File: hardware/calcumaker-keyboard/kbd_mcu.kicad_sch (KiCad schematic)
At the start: 8 parts, among them J2 SWD TC2030-NL, U1 STM32G031K8U6

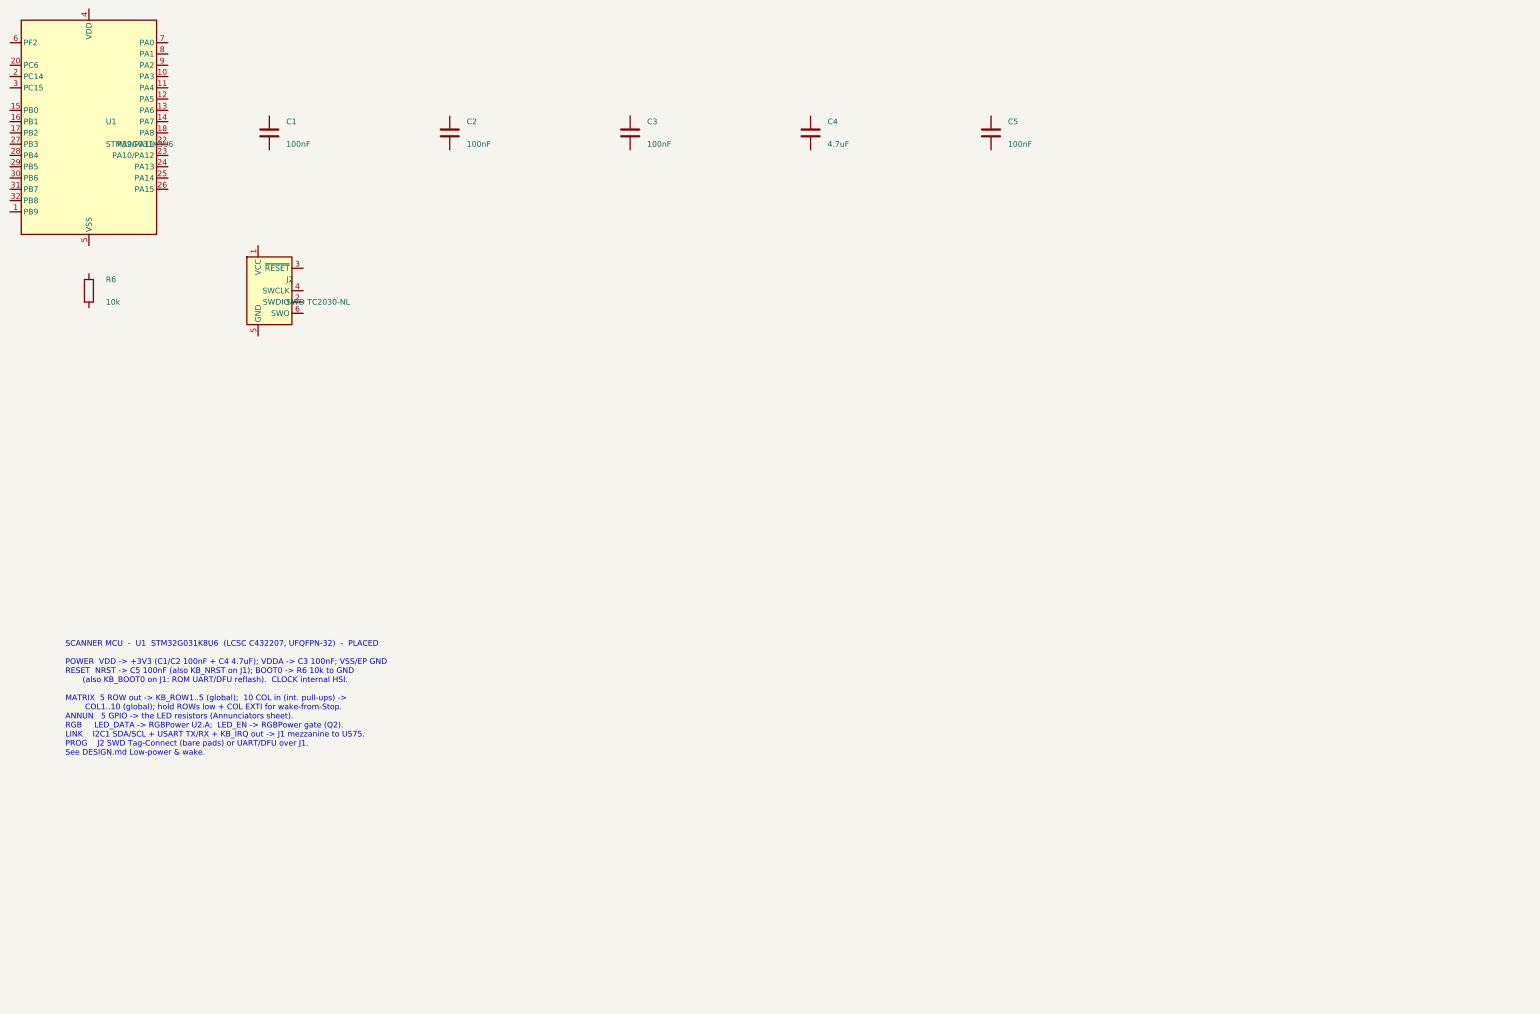
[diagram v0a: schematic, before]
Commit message: Wire mainboard and keypad schematics and verify expanded nets
Connect hierarchical interfaces, power/control circuits, debug links, matrix and RGB chains. Correct MCU package pins, diode polarity and power configuration; add bypass components and repeatable KiCad netlist/ERC checks. Document pin maps and remaining physical validation.
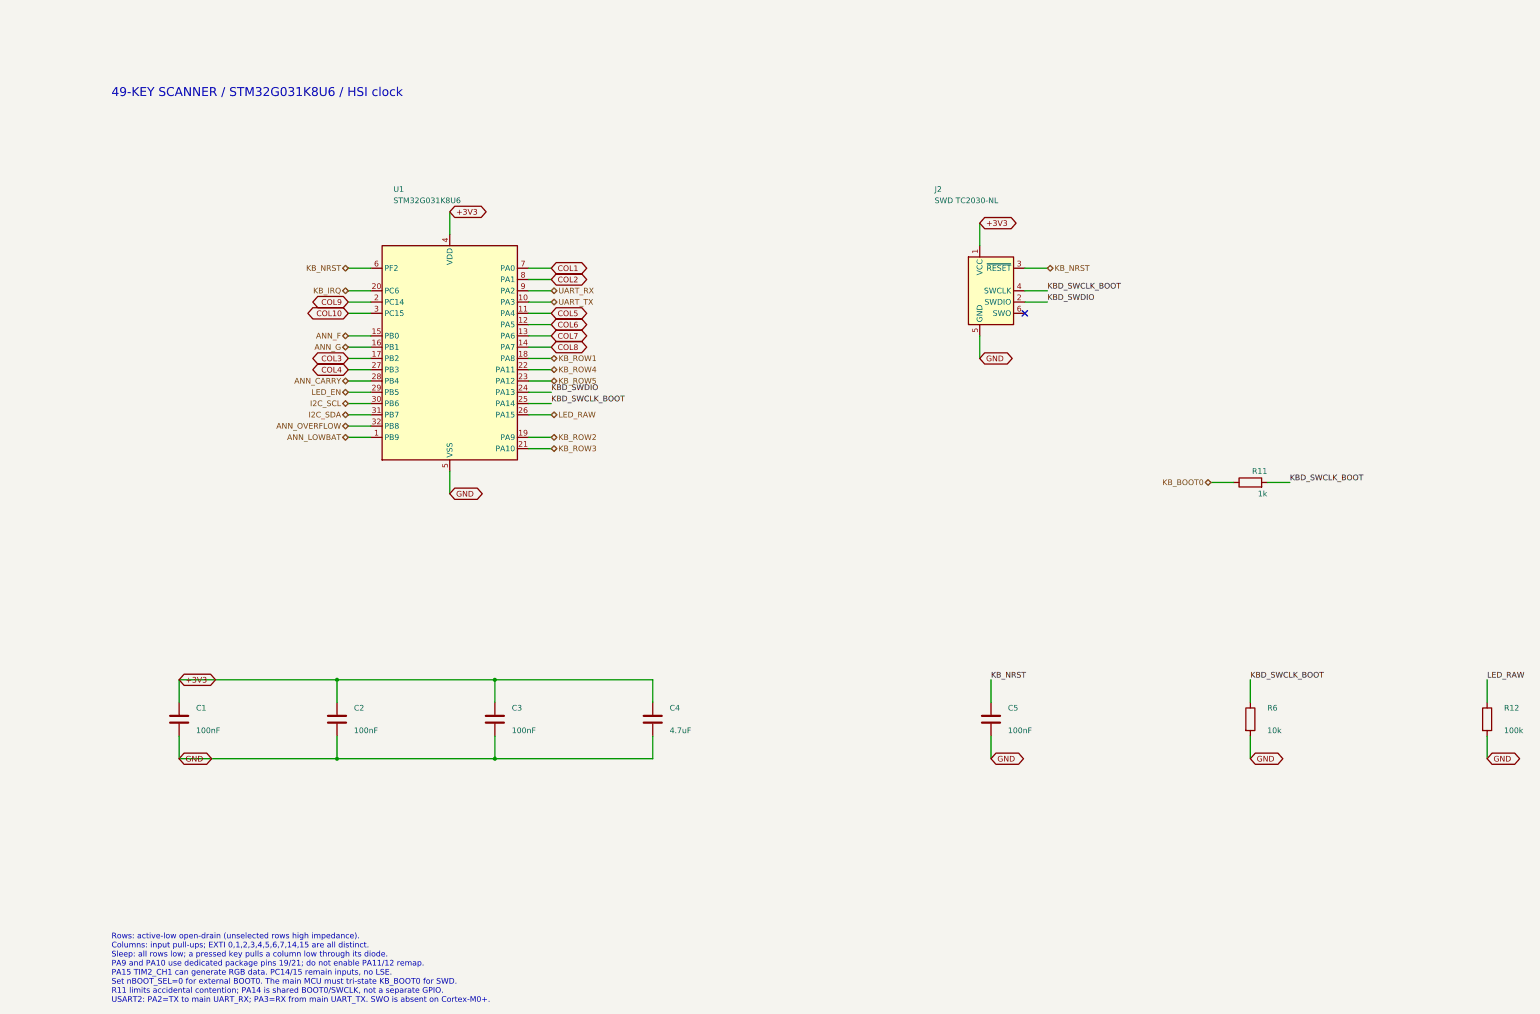
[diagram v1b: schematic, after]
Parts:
- added R11: 1k, Resistor_SMD:R_0402_1005Metric, symbol Device:R
- added R12: 100k, Resistor_SMD:R_0402_1005Metric, symbol Device:R
- U1: symbol MCU_ST_STM32G0:STM32G031K8Ux -> calcumaker:STM32G031K8U6
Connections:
- net +3V3: now reaches C2.1
- net +3V3: now also C1.1, C3.1, C4.1, J2.1 (VCC), U1.4 (VDD)
- net GND: now reaches C2.2
- net GND: now also C1.2, C3.2, C4.2, C5.2, J2.5 (GND), R6.2, U1.33 (VSS), U1.5 (VSS), R12.2
- net KBD_SWDIO: now reaches J2.2 (SWDIO)
- net KBD_SWDIO: now also U1.24 (PA13)
- net KB_NRST: now reaches J2.3 (~{RESET})
- net KB_NRST: now also C5.1, U1.6 (PF2)
- net KBD_SWCLK_BOOT: now reaches J2.4 (SWCLK)
- net KBD_SWCLK_BOOT: now also R6.1, U1.25 (PA14), R11.2
- net ANN_LOWBAT: now reaches U1.1 (PB9)
- net UART_TX: now reaches U1.10 (PA3)
- net COL5: now reaches U1.11 (PA4)
- net COL6: now reaches U1.12 (PA5)
- net COL7: now reaches U1.13 (PA6)
- net COL8: now reaches U1.14 (PA7)
- net ANN_F: now reaches U1.15 (PB0)
- net ANN_G: now reaches U1.16 (PB1)
- net COL3: now reaches U1.17 (PB2)
- net KB_ROW1: now reaches U1.18 (PA8)
- net KB_ROW2: now reaches U1.19 (PA9)
- net COL9: now reaches U1.2 (PC14)
- net KB_IRQ: now reaches U1.20 (PC6)
- net KB_ROW3: now reaches U1.21 (PA10)
- net KB_ROW4: now reaches U1.22 (PA11)
- net KB_ROW5: now reaches U1.23 (PA12)
- net LED_RAW: now reaches U1.26 (PA15)
- net LED_RAW: now also R12.1
- net COL4: now reaches U1.27 (PB3)
- net ANN_CARRY: now reaches U1.28 (PB4)
- net LED_EN: now reaches U1.29 (PB5)
- net COL10: now reaches U1.3 (PC15)
- net I2C_SCL: now reaches U1.30 (PB6)
- net I2C_SDA: now reaches U1.31 (PB7)
- net ANN_OVERFLOW: now reaches U1.32 (PB8)
- net COL1: now reaches U1.7 (PA0)
- net COL2: now reaches U1.8 (PA1)
- net UART_RX: now reaches U1.9 (PA2)
- new net KB_BOOT0: R11.1
- no-connect marks 0 -> 1
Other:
- note added: "49-KEY SCANNER / STM32G031K8U6 / HSI clock"
- note added: "Rows: active-low open-drain (unselected rows high impedance). Columns: input pull-ups; EXTI 0,1,2,3,4,5,6,7,14,15 are all distinct. Sleep: all rows low; a pressed key pulls a column low through its diode. PA9 and PA10 use dedicated package pins 19/21; do not enable PA11/12 remap. PA15 TIM2_CH1 can generate RGB data. PC14/15 remain inputs, no LSE. Set nBOOT_SEL=0 for external BOOT0. The main MCU m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"
- note removed: "SCANNER MCU - U1 STM32G031K8U6 (LCSC C432207, UFQFPN-32) - PLACED POWER VDD -> +3V3 (C1/C2 100nF + C4 4.7uF); VDDA -> C3 100nF; VSS/EP GND RESET NRST -> C5 100nF (also KB_NRST on J1); BOOT0 -> R6 10k to GND (also KB_BOOT0 on J1: ROM UART/DFU reflash). CLOCK internal HSI. MATRIX 5 ROW out -> KB_ROW1..5 (global); 10 COL in (int. pull-ups) -> COL1..10 (global); hold ROWs low + COL EXTI for wake-from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"
- title: Calcumaker 16 — Keyboard — Keyboard scanner MCU (STM32G031K8U6) -> Calcumaker 16 / keyboard / kbd mcu
- moved on the sheet: C1, C2, C3, C4, C5, J2, R6
